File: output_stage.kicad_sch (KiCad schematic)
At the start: 36 parts, among them J6 RAIL_POL, J7 OUTPUT, J8 RAIL_POL, J9 OUTPUT, K1 HFD4-3, K2 HFD4-3, Q5 DMG2302U, Q6 DMG2302U, U16 INA180A4, U17 INA180A4

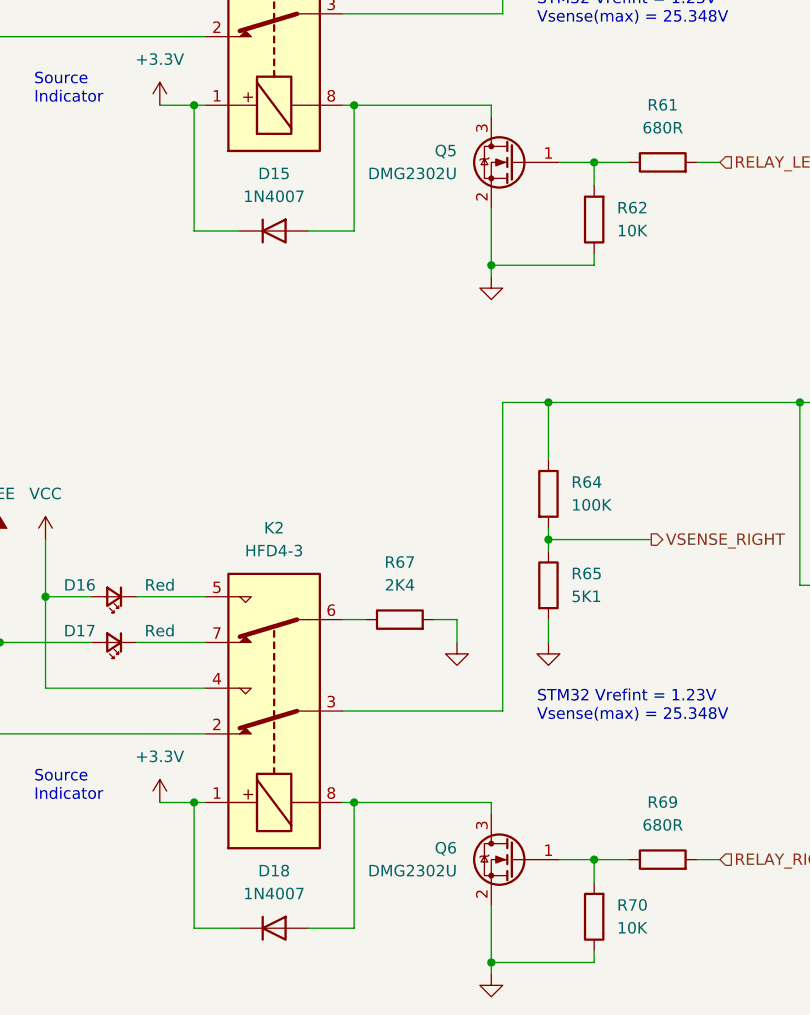
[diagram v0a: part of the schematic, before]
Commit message: Power optimization, add Aisler Assembly MPN info
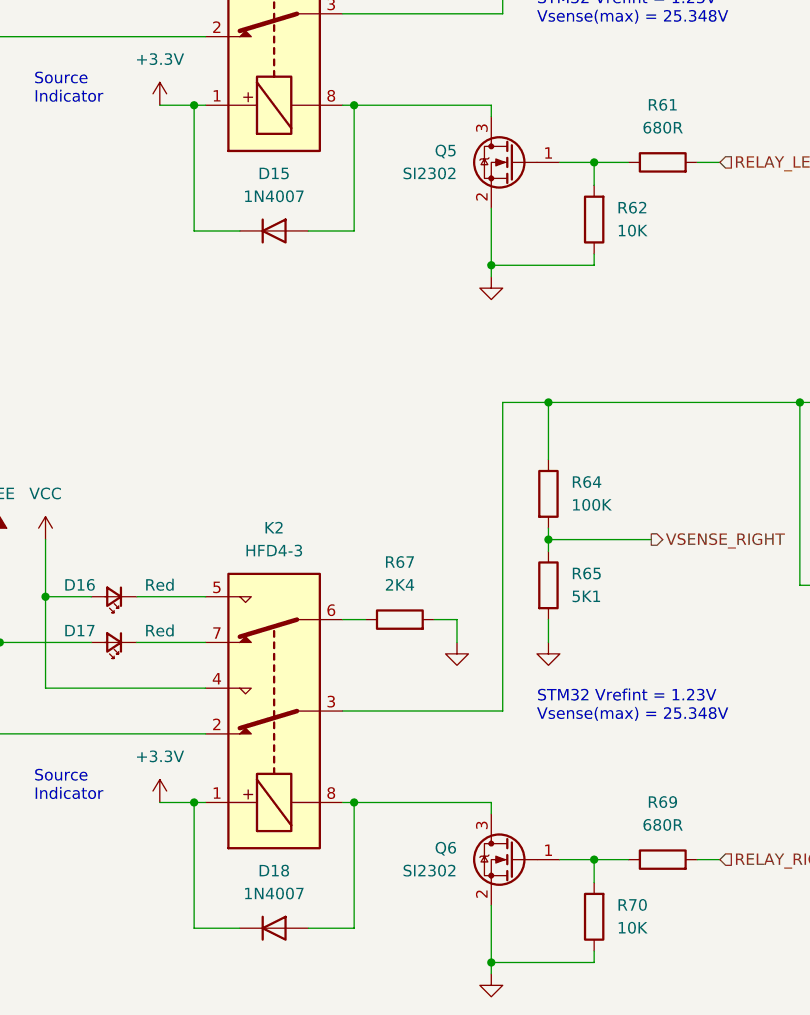
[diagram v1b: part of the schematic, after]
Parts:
- C45, C47: MPN (none) -> 100nF 50V X7R
- D13, D14, D16, D17: MPN (none) -> KT-0603R
- D15, D18: MPN (none) -> A7
- K1, K2: MPN (none) -> HFD4/3-SR
- Q5, Q6: value DMG2302U -> SI2302; MPN (none) -> SI2302
- R55, R63: MPN (none) -> 1m5R 1%
- R56, R64: MPN (none) -> 100K 1%
- R57, R65: MPN (none) -> 5K1 1%
- R58, R60, R66, R68: MPN (none) -> 0R 1%
- R59, R67: MPN (none) -> 2K4 1%
- R61, R69: MPN (none) -> 680R 1%
- R62, R70: MPN (none) -> 10K 1%
- U16, U17: MPN (none) -> INA180A4IDBVR
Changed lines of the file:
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@@
+      (effects (font (size 1.27 1.27)) hide)
+    )
+    (property "MPN" "680R 1%" (id 4) (at 105.41 80.01 0)
       (effects (font (size 1.27 1.27)) hide)
     )
@@
       (effects (font (size 1.27 1.27)) hide)
     )
+    (property "MPN" "1m5R 1%" (id 4) (at 125.73 29.21 0)
+      (effects (font (size 1.27 1.27)) hide)
+    )
     (pin "1")
     (pin "2")
@@
     )
     (property "Datasheet" "https://datasheet.lcsc.com/lcsc/1809291515_HF-Xiamen-Hongfa-Electroacoustic-HFD4-3_C119084.pdf" (id 3) (at 62.23 63.5 0)
+      (effects (font (size 1.27 1.27)) hide)
+    )
+    (property "MPN" "HFD4/3-SR" (id 4) (at 62.23 63.5 0)
       (effects (font (size 1.27 1.27)) hide)
     )
@@
       (effects (font (size 1.27 1.27)) hide)
     )
+    (property "MPN" "0R 1%" (id 4) (at 135.89 54.61 0)
+      (effects (font (size 1.27 1.27)) hide)
+    )
     (pin "1")
     (pin "2")
@@
       (effects (font (size 1.27 1.27)) hide)
     )
+    (property "MPN" "KT-0603R" (id 4) (at 43.18 50.8 0)
+      (effects (font (size 1.27 1.27)) hide)
+    )
     (pin "1")
     (pin "2")
@@
       (effects (font (size 1.27 1.27)) hide)
     )
+    (property "MPN" "A7" (id 4) (at 62.23 165.1 0)
+      (effects (font (size 1.27 1.27)) hide)
+    )
     (pin "1")
     (pin "2")
@@
       (effects (font (size 1.27 1.27)) hide)
     )
+    (property "MPN" "10K 1%" (id 4) (at 97.79 163.83 0)
+      (effects (font (size 1.27 1.27)) hide)
+    )
     (pin "1")
     (pin "2")
@@
     )
     (property "Datasheet" "~" (id 3) (at 92.71 49.53 0)
+      (effects (font (size 1.27 1.27)) hide)
+    )
+    (property "MPN" "5K1 1%" (id 4) (at 92.71 49.53 0)
       (effects (font (size 1.27 1.27)) hide)
     )
@@
       (effects (font (size 1.27 1.27)) hide)
     )
+    (property "MPN" "INA180A4IDBVR" (id 4) (at 162.56 129.54 0)
+      (effects (font (size 1.27 1.27)) hide)
+    )
     (pin "1")
     (pin "2")
@@
       (effects (font (size 1.27 1.27)) hide)
     )
+    (property "MPN" "KT-0603R" (id 4) (at 43.18 55.88 0)
+      (effects (font (size 1.27 1.27)) hide)
+    )
     (pin "1")
     (pin "2")
@@
       (effects (font (size 1.27 1.27)) hide)
     )
+    (property "MPN" "680R 1%" (id 4) (at 105.41 157.48 0)
+      (effects (font (size 1.27 1.27)) hide)
+    )
     (pin "1")
     (pin "2")
@@
       (effects (font (size 1.27 1.27)) hide)
     )
+    (property "MPN" "0R 1%" (id 4) (at 135.89 127 0)
+      (effects (font (size 1.27 1.27)) hide)
+    )
     (pin "1")
     (pin "2")
@@
       (effects (font (size 1.27 1.27)) (justify left))
     )
-    (property "Value" "DMG2302U" (id 1) (at 82.55 158.7499 0)
+    (property "Value" "SI2302" (id 1) (at 82.55 158.7499 0)
       (effects (font (size 1.27 1.27)) (justify left))
     )
@@
     (property "Datasheet" "http://www.diodes.com/assets/Datasheets/DMG2302U.pdf" (id 3) (at 88.9 157.48 0)
       (effects (font (size 1.27 1.27)) (justify left) hide)
+    )
+    (property "MPN" "SI2302" (id 4) (at 88.9 157.48 0)
+      (effects (font (size 1.27 1.27)) hide)
     )
     (pin "1")
@@
       (effects (font (size 1.27 1.27)) hide)
     )
+    (property "MPN" "KT-0603R" (id 4) (at 44.45 128.27 0)
+      (effects (font (size 1.27 1.27)) hide)
+    )
     (pin "1")
     (pin "2")
@@
       (effects (font (size 1.27 1.27)) hide)
     )
+    (property "MPN" "2K4 1%" (id 4) (at 76.2 130.81 0)
+      (effects (font (size 1.27 1.27)) hide)
+    )
     (pin "1")
     (pin "2")
@@
       (effects (font (size 1.27 1.27)) hide)
     )
+    (property "MPN" "1m5R 1%" (id 4) (at 125.73 106.68 0)
+      (effects (font (size 1.27 1.27)) hide)
+    )
     (pin "1")
     (pin "2")
@@
     )
     (property "Datasheet" "~" (id 3) (at 92.71 127 0)
+      (effects (font (size 1.27 1.27)) hide)
+    )
+    (property "MPN" "5K1 1%" (id 4) (at 92.71 127 0)
       (effects (font (size 1.27 1.27)) hide)
     )
@@
       (effects (font (size 1.27 1.27)) hide)
     )
+    (property "MPN" "A7" (id 4) (at 62.23 87.63 0)
+      (effects (font (size 1.27 1.27)) hide)
+    )
     (pin "1")
     (pin "2")
@@
       (effects (font (size 1.27 1.27)) hide)
     )
+    (property "MPN" "100K 1%" (id 4) (at 92.71 39.37 0)
+      (effects (font (size 1.27 1.27)) hide)
+    )
     (pin "1")
     (pin "2")
@@
     )
     (property "Datasheet" "~" (id 3) (at 92.71 116.84 0)
+      (effects (font (size 1.27 1.27)) hide)
+    )
+    (property "MPN" "100K 1%" (id 4) (at 92.71 116.84 0)
       (effects (font (size 1.27 1.27)) hide)
     )
@@
     )
     (property "Datasheet" "http://www.ti.com/lit/ds/symlink/ina180.pdf" (id 3) (at 166.37 48.26 0)
+      (effects (font (size 1.27 1.27)) hide)
+    )
+    (property "MPN" "INA180A4IDBVR" (id 4) (at 162.56 52.07 0)
       (effects (font (size 1.27 1.27)) hide)
     )
@@
       (effects (font (size 1.27 1.27)) hide)
     )
+    (property "MPN" "10K 1%" (id 4) (at 97.79 86.36 0)
+      (effects (font (size 1.27 1.27)) hide)
+    )
     (pin "1")
     (pin "2")
@@
     )
     (property "Datasheet" "https://datasheet.lcsc.com/lcsc/1809291515_HF-Xiamen-Hongfa-Electroacoustic-HFD4-3_C119084.pdf" (id 3) (at 62.23 140.97 0)
+      (effects (font (size 1.27 1.27)) hide)
+    )
+    (property "MPN" "HFD4/3-SR" (id 4) (at 62.23 140.97 0)
       (effects (font (size 1.27 1.27)) hide)
     )
@@
       (effects (font (size 1.27 1.27)) (justify left))
     )
-    (property "Value" "DMG2302U" (id 1) (at 82.55 81.2799 0)
+    (property "Value" "SI2302" (id 1) (at 82.55 81.2799 0)
       (effects (font (size 1.27 1.27)) (justify left))
     )
@@
     (property "Datasheet" "http://www.diodes.com/assets/Datasheets/DMG2302U.pdf" (id 3) (at 88.9 80.01 0)
       (effects (font (size 1.27 1.27)) (justify left) hide)
+    )
+    (property "MPN" "SI2302" (id 4) (at 88.9 80.01 0)
+      (effects (font (size 1.27 1.27)) hide)
     )
     (pin "1")
@@
       (effects (font (size 1.27 1.27)) hide)
     )
+    (property "MPN" "0R 1%" (id 4) (at 135.89 49.53 0)
+      (effects (font (size 1.27 1.27)) hide)
+    )
     (pin "1")
     (pin "2")
@@
     )
     (property "Datasheet" "~" (id 3) (at 168.91 40.64 0)
+      (effects (font (size 1.27 1.27)) hide)
+    )
+    (property "MPN" "100nF 50V X7R" (id 4) (at 168.91 40.64 0)
       (effects (font (size 1.27 1.27)) hide)
     )
@@
       (effects (font (size 1.27 1.27)) hide)
     )
+    (property "MPN" "0R 1%" (id 4) (at 135.89 132.08 0)
+      (effects (font (size 1.27 1.27)) hide)
+    )
     (pin "1")
     (pin "2")
@@
       (effects (font (size 1.27 1.27)) hide)
     )
+    (property "MPN" "KT-0603R" (id 4) (at 44.45 133.35 0)
+      (effects (font (size 1.27 1.27)) hide)
+    )
     (pin "1")
     (pin "2")
@@
     )
     (property "Datasheet" "~" (id 3) (at 168.91 118.11 0)
+      (effects (font (size 1.27 1.27)) hide)
+    )
+    (property "MPN" "100nF 50V X7R" (id 4) (at 168.91 118.11 0)
       (effects (font (size 1.27 1.27)) hide)
     )
@@
       (effects (font (size 1.27 1.27)) hide)
     )
+    (property "MPN" "2K4 1%" (id 4) (at 76.2 53.34 0)
+      (effects (font (size 1.27 1.27)) hide)
+    )

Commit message: Create IBOM, Add sheet info
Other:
- company: (none) -> Sleepy Pony Labs
- title: (none) -> Dual Rail Breadboard Power Supply
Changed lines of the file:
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@@
 (kicad_sch (version 20211123) (generator eeschema)
   (paper "A4")
+  (title_block
+    (title "Dual Rail Breadboard Power Supply")
+    (date "2023-06-11")
+    (rev "1")
+    (company "Sleepy Pony Labs")
+  )
   (junction (at 36.83 50.8) (diameter 0) (color 0 0 0 0)
   )
